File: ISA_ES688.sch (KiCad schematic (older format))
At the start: 104 parts, among them J1 LINE IN, J11 ISA BUS, J2 LINE OUT, J3 Joystick/MIDI, J7 SPKR OUT, J8 MIC, U1 L78L05, U2 74LS14, U7 LM1877, Y1 14.318Mhz

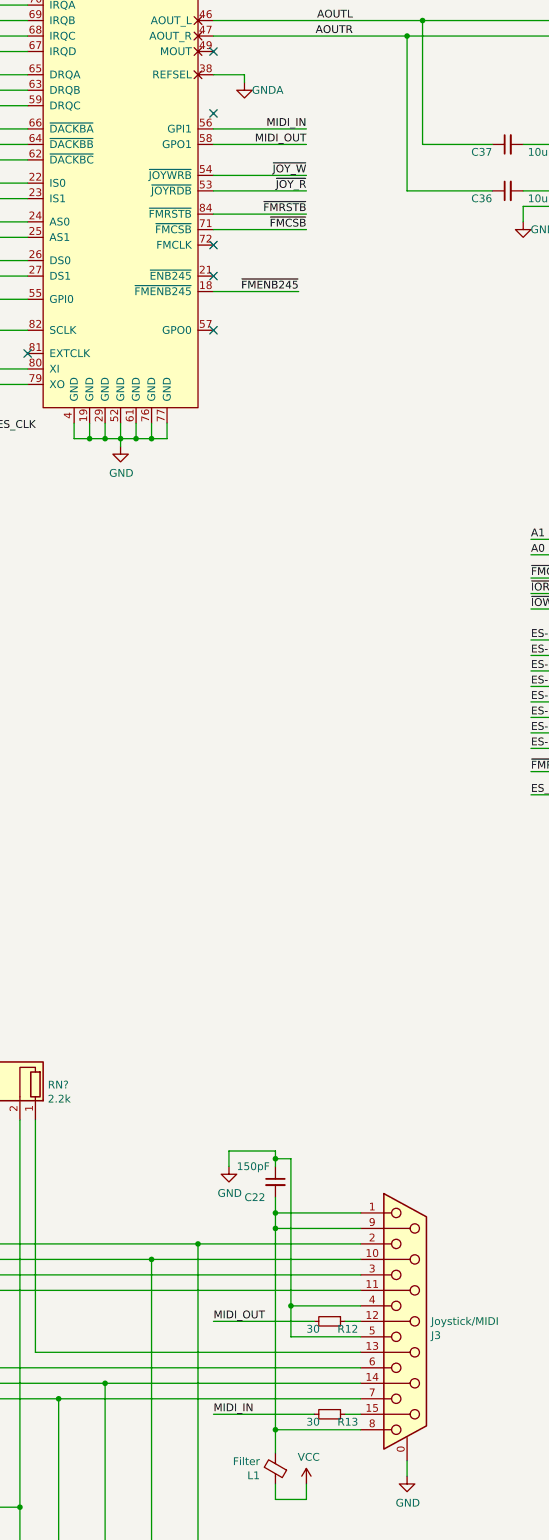
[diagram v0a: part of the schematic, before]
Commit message: Rewire midi connection
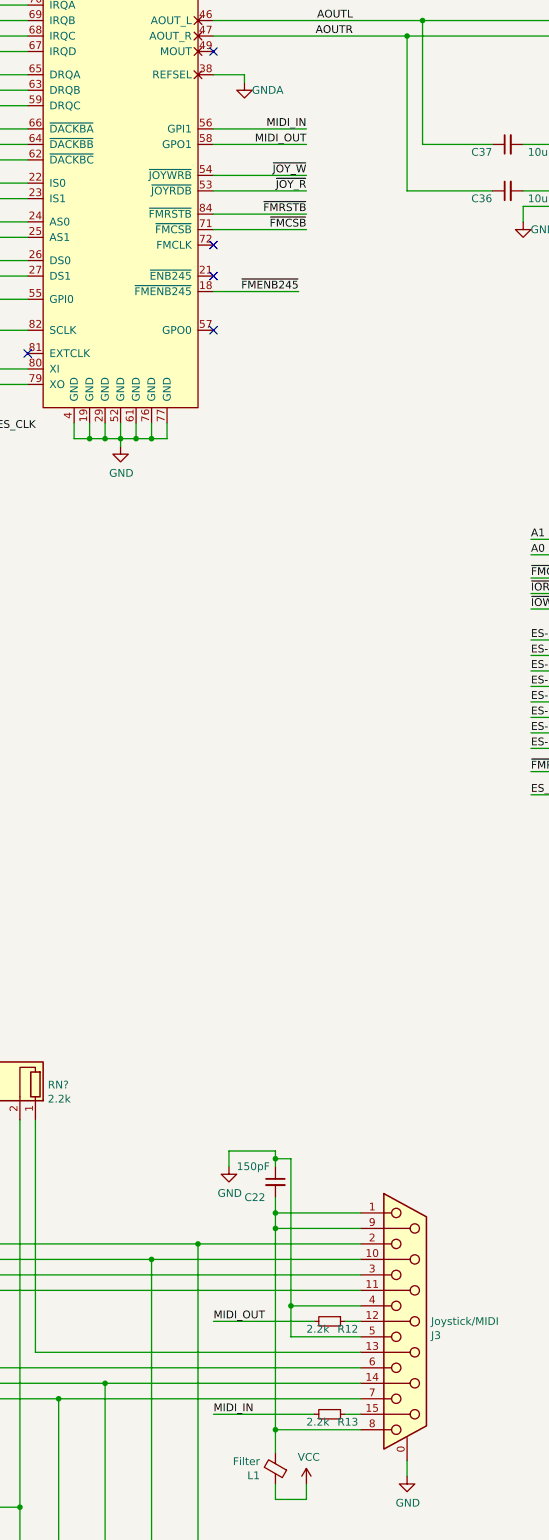
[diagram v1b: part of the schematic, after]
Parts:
- R12, R13: value 30 -> 2.2k
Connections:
- no-connect marks 33 -> 32
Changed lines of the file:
@@
 P 13350 13550
 F 0 "R13" V 13400 13600 50  0000 L CNN
-F 1 "30" V 13400 13400 50  0000 L CNN
+F 1 "2.2k" V 13400 13400 50  0000 L CNN
 F 2 "Resistor_THT:R_Axial_DIN0207_L6.3mm_D2.5mm_P7.62mm_Horizontal" H 13350 13550 50  0001 C CNN
 F 3 "~" H 13350 13550 50  0001 C CNN
@@
 P 13350 12950
 F 0 "R12" V 13400 13000 50  0000 L CNN
-F 1 "30" V 13400 12800 50  0000 L CNN
+F 1 "2.2k" V 13400 12800 50  0000 L CNN
 F 2 "Resistor_THT:R_Axial_DIN0207_L6.3mm_D2.5mm_P7.62mm_Horizontal" H 13350 12950 50  0001 C CNN
 F 3 "~" H 13350 12950 50  0001 C CNN
@@
 Text Notes 20850 10100 0    50   ~ 0
 C24 measured out of circuit as 160nF
-NoConn ~ 12600 5150
 $EndSCHEMATC

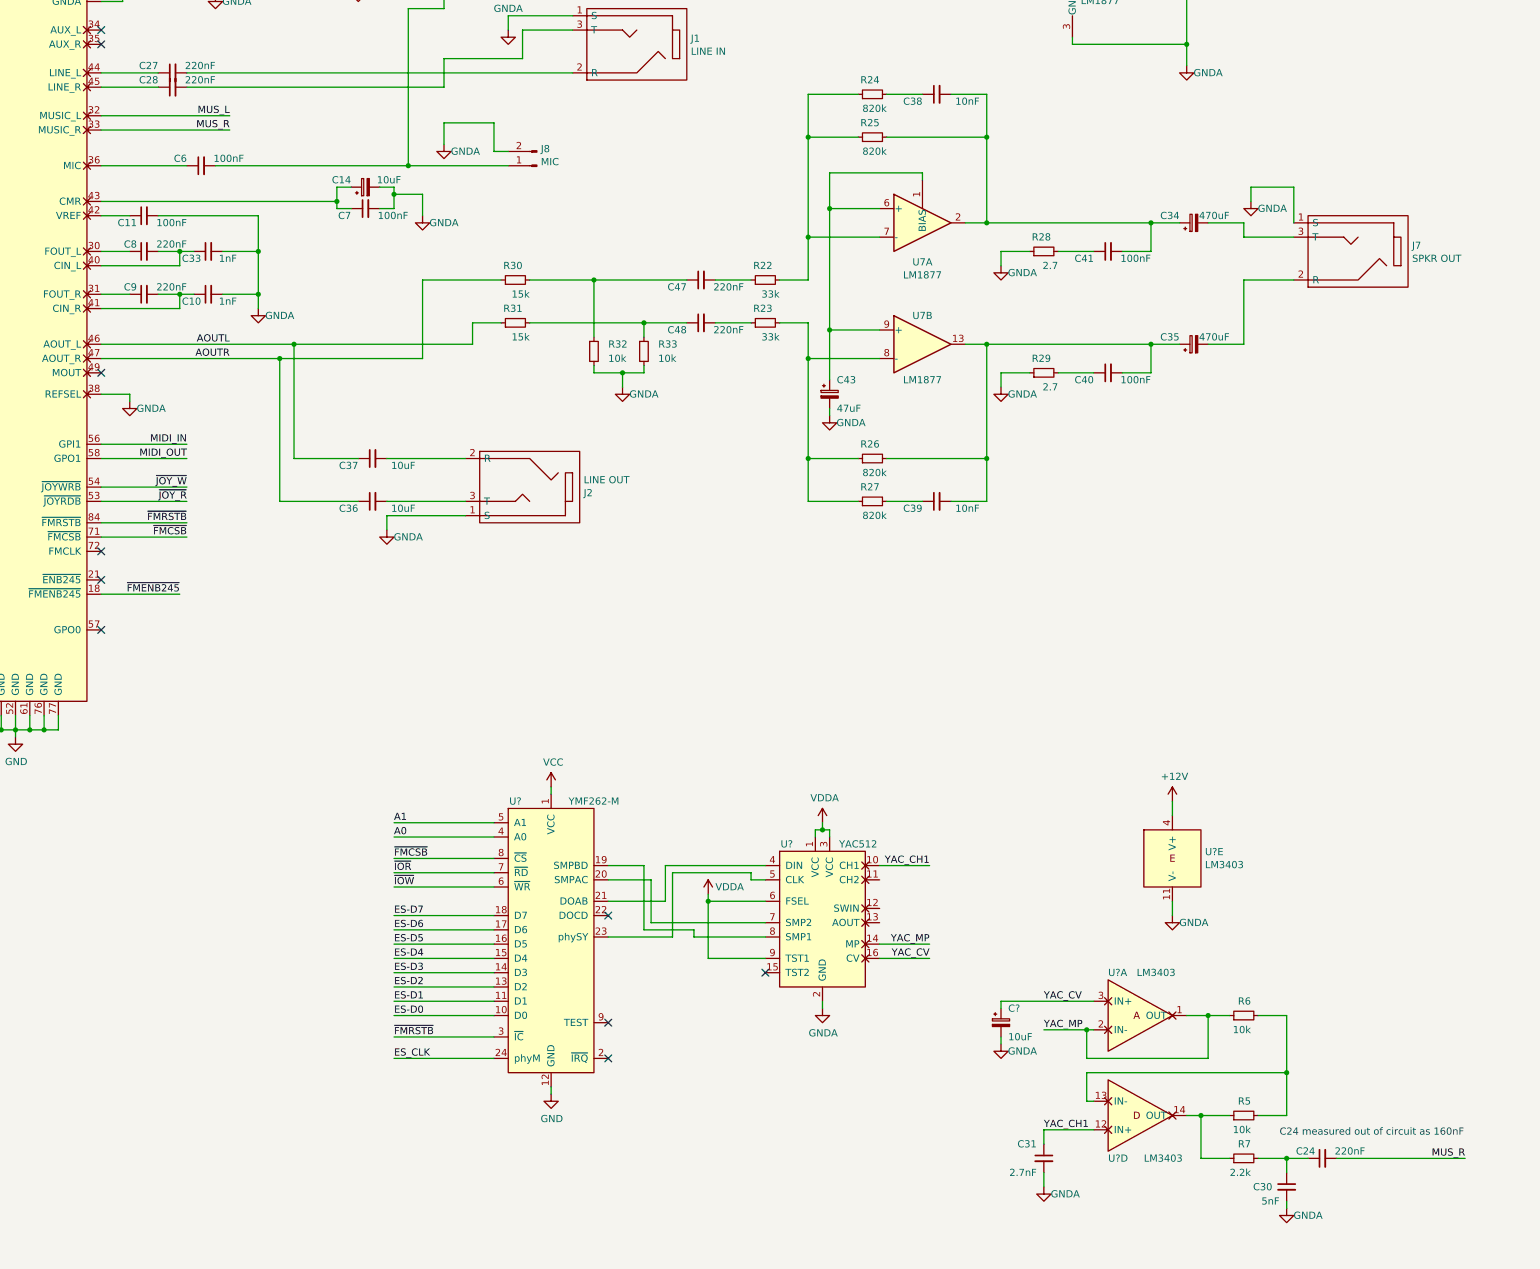
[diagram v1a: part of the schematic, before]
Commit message: Reorganize connections a bit
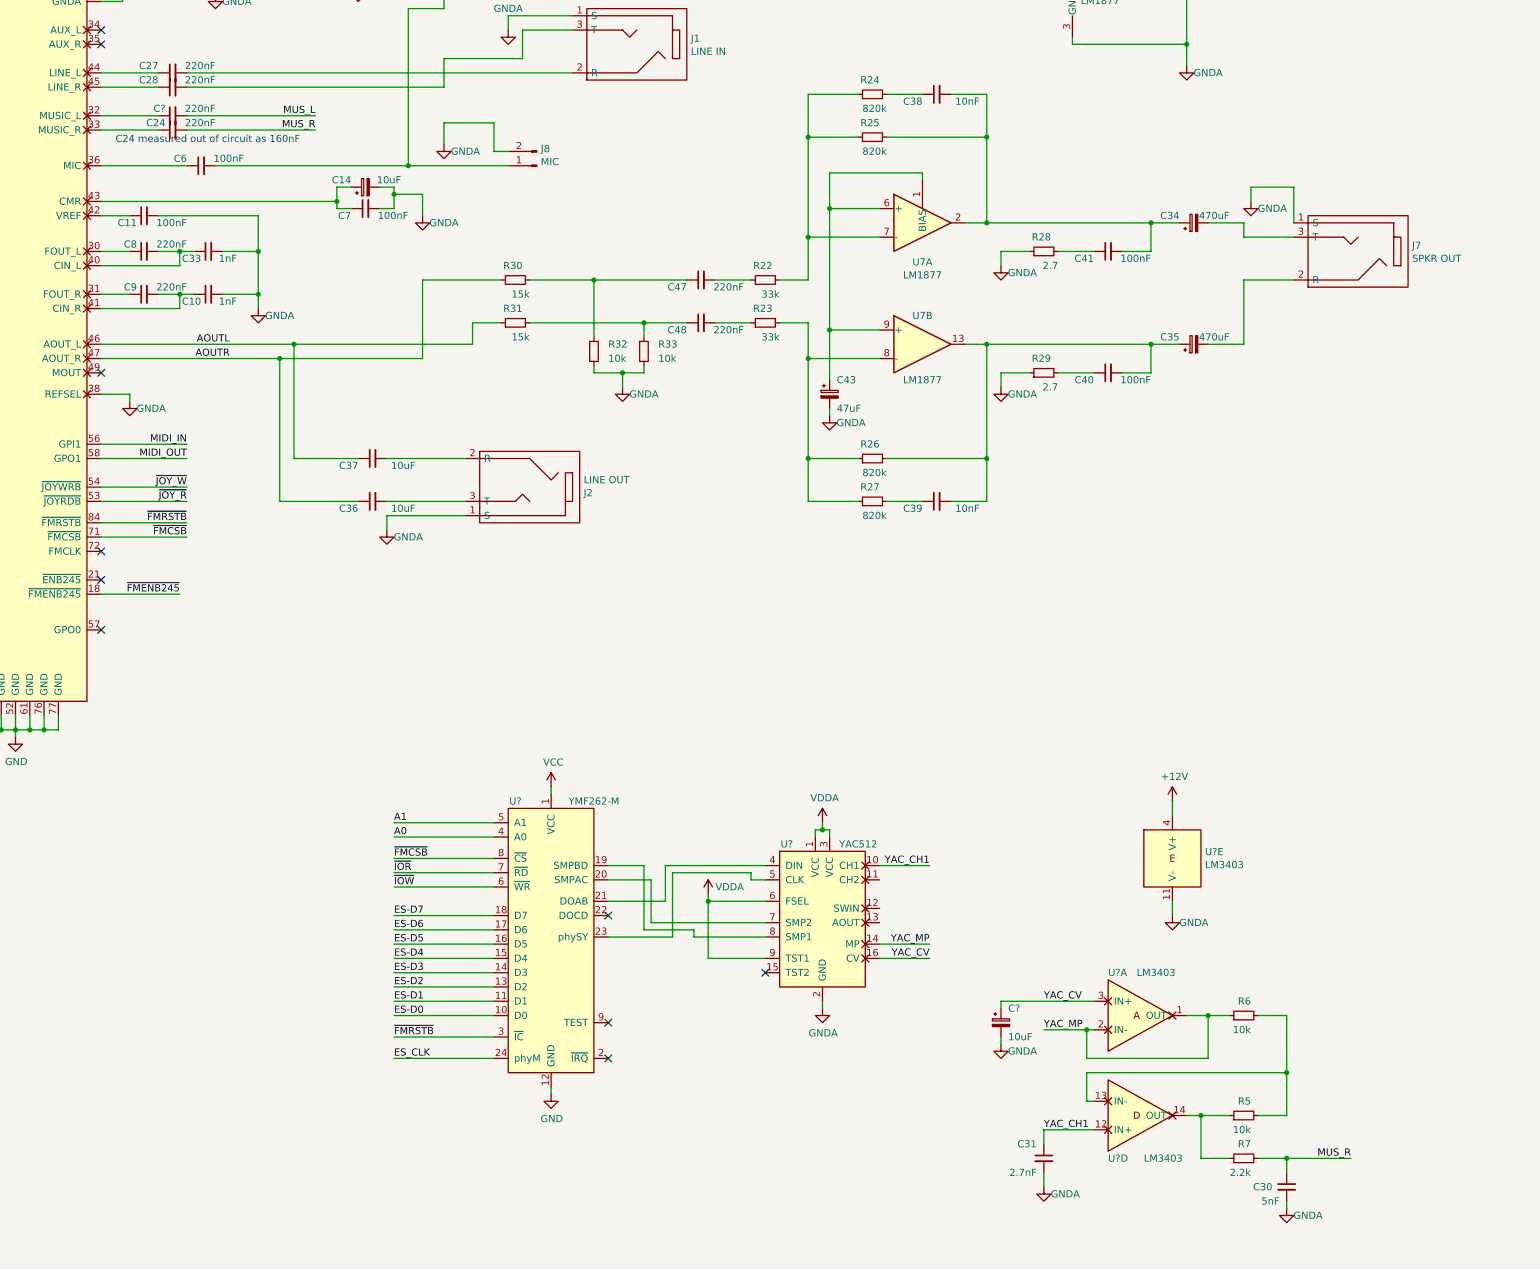
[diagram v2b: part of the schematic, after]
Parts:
- added C?: 220nF, Capacitor_THT:C_Disc_D6.0mm_W2.5mm_P5.00mm, symbol Device:C_Small
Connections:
- net MUS_L: now also C?.2; no longer U?.32 (MUSIC_L)
- net MUS_R: now also C30.1, R7.2; no longer U?.33 (MUSIC_R)
- new net: C?.1, U?.32 (MUSIC_L)
- new net: C24.1, U?.33 (MUSIC_R)
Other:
- moved on the sheet: C24
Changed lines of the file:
@@
 NoConn ~ 12600 2450
 Wire Wire Line
-	12600 2950 13500 2950
-Wire Wire Line
-	12600 3050 13500 3050
-Text Label 13500 2950 2    50   ~ 0
+	13200 2950 14100 2950
+Wire Wire Line
+	13200 3050 14100 3050
+Text Label 14100 2950 2    50   ~ 0
 MUS_L
-Text Label 13500 3050 2    50   ~ 0
+Text Label 14100 3050 2    50   ~ 0
 MUS_R
 NoConn ~ 12600 6200
@@
 L Device:C_Small C24
 U 1 1 62A6A051
-P 21150 10250
-F 0 "C24" V 21100 10300 50  0000 L CNN
-F 1 "220nF" V 21100 9950 50  0000 L CNN
-F 2 "Capacitor_THT:C_Disc_D6.0mm_W2.5mm_P5.00mm" H 21150 10250 50  0001 C CNN
-F 3 "~" H 21150 10250 50  0001 C CNN
-	1    21150 10250
+P 13100 3050
+F 0 "C24" V 13050 3100 50  0000 L CNN
+F 1 "220nF" V 13050 2750 50  0000 L CNN
+F 2 "Capacitor_THT:C_Disc_D6.0mm_W2.5mm_P5.00mm" H 13100 3050 50  0001 C CNN
+F 3 "~" H 13100 3050 50  0001 C CNN
+	1    13100 3050
 	0    -1   1    0
 $EndComp
-Wire Wire Line
-	20900 10250 21050 10250
-Connection ~ 20900 10250
-Wire Wire Line
-	21250 10250 22150 10250
-Text Label 22150 10250 2    50   ~ 0
+Text Label 21350 10250 2    50   ~ 0
 MUS_R
 Wire Wire Line
@@
 Wire Wire Line
 	19200 10050 19200 10150
-Text Notes 20850 10100 0    50   ~ 0
+Text Notes 12700 3150 0    50   ~ 0
 C24 measured out of circuit as 160nF
+$Comp
+L Device:C_Small C?
+U 1 1 61F8B525
+P 13100 2950
+F 0 "C?" V 13050 3000 50  0000 L CNN
+F 1 "220nF" V 13050 2650 50  0000 L CNN
+F 2 "Capacitor_THT:C_Disc_D6.0mm_W2.5mm_P5.00mm" H 13100 2950 50  0001 C CNN
+F 3 "~" H 13100 2950 50  0001 C CNN
+	1    13100 2950
+	0    -1   1    0
+$EndComp
+Wire Wire Line
+	12600 2950 13000 2950
+Wire Wire Line
+	13000 3050 12600 3050
+Wire Wire Line
+	20900 10250 21350 10250
+Connection ~ 20900 10250
 $EndSCHEMATC

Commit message: More OP-AMP circuit
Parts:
- removed JP?: Emulation Mode, symbol Device:Jumper_NO_Small
- removed R?: 10k, Resistor_THT:R_Axial_DIN0207_L6.3mm_D2.5mm_P7.62mm_Horizontal, symbol Device:R_Small
- added C26: 33-68pF, Capacitor_THT:C_Disc_D6.0mm_W2.5mm_P5.00mm, symbol Device:C_Small
- added JP?: Emulation Mode, symbol Jumper:Jumper_3_Open
- added R1: 33, Resistor_THT:R_Axial_DIN0207_L6.3mm_D2.5mm_P7.62mm_Horizontal, symbol Device:R_Small
- C14: value 10uF -> 47uF
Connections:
- net GND: now also JP?.1 (A)
- net GNDA: now also C26.1
- net VCC: now also JP?.3 (B)
- net at U?.55 (GPI0): now also JP?.2 (C)
- net YAC_AOUT: now reaches U?.5 (IN+)
- net YAC_AOUT: now also U?.13 (AOUT), C26.2
- net at U?.6 (IN-): now also U?.7 (OUT), R1.2
- net YAC_CH2: now reaches U?.11 (CH2)
- net YAC_SWIN: now reaches U?.12 (SWIN)
- net YAC_SWIN: now also R1.1
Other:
- note added: "1-2: Sound Blaster v2.11\n2-3: Sound Blaster PRO v3.1"
- note removed: "Defaults to\nSound Blaster PRO"
- moved on the sheet: U?C
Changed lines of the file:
@@
 P 14450 3450
 F 0 "C14" V 14500 3550 50  0000 L CNN
-F 1 "10uF" V 14500 3200 50  0000 L CNN
+F 1 "47uF" V 14500 3200 50  0000 L CNN
 F 2 "Capacitor_THT:CP_Radial_D5.0mm_P2.50mm" H 14450 3450 50  0001 C CNN
 F 3 "~" H 14450 3450 50  0001 C CNN
@@
 	11100 6700 11100 6550
 $Comp
-L Device:R_Small R?
-U 1 1 624E2824
-P 10550 6550
-F 0 "R?" H 10400 6500 50  0000 L CNN
-F 1 "10k" H 10350 6600 50  0000 L CNN
-F 2 "Resistor_THT:R_Axial_DIN0207_L6.3mm_D2.5mm_P7.62mm_Horizontal" H 10550 6550 50  0001 C CNN
-F 3 "~" H 10550 6550 50  0001 C CNN
-	1    10550 6550
-	-1   0    0    1
-$EndComp
-Wire Wire Line
-	11400 6350 10550 6350
-Wire Wire Line
-	10550 6350 10550 6450
-Wire Wire Line
-	10550 6650 10550 6700
-Wire Wire Line
-	10550 6700 10850 6700
-Connection ~ 10850 6700
-$Comp
-L Device:Jumper_NO_Small JP?
-U 1 1 626D2891
-P 10350 6350
-F 0 "JP?" H 10350 6250 50  0000 C CNN
-F 1 "Emulation Mode" H 10350 6444 50  0000 C CNN
-F 2 "" H 10350 6350 50  0001 C CNN
-F 3 "~" H 10350 6350 50  0001 C CNN
-	1    10350 6350
-	1    0    0    -1
-$EndComp
-Wire Wire Line
-	10450 6350 10550 6350
-Connection ~ 10550 6350
-$Comp
 L power:GND #PWR?
 U 1 1 6271B50D
-P 10150 6500
-F 0 "#PWR?" H 10150 6250 50  0001 C CNN
-F 1 "GND" H 10155 6327 50  0000 C CNN
-F 2 "" H 10150 6500 50  0001 C CNN
-F 3 "" H 10150 6500 50  0001 C CNN
-	1    10150 6500
-	1    0    0    -1
-$EndComp
-Wire Wire Line
-	10250 6350 10150 6350
-Wire Wire Line
-	10150 6350 10150 6500
-Text Notes 10050 6500 2    50   ~ 0
-Defaults to\nSound Blaster PRO
+P 9750 7100
+F 0 "#PWR?" H 9750 6850 50  0001 C CNN
+F 1 "GND" H 9755 6927 50  0000 C CNN
+F 2 "" H 9750 7100 50  0001 C CNN
+F 3 "" H 9750 7100 50  0001 C CNN
+	1    9750 7100
+	1    0    0    -1
+$EndComp
 Wire Wire Line
 	11400 4450 10900 4450
@@
 L custom_components:LM3403 U?
 U 3 1 6191F91E
-P 19950 12200
-F 0 "U?" H 19750 12500 50  0000 L CNN
-F 1 "LM3403" H 19950 12500 50  0000 L CNN
-F 2 "" H 19950 12200 50  0001 C CNN
-F 3 "" H 19950 12200 50  0001 C CNN
-	3    19950 12200
+P 19950 12500
+F 0 "U?" H 19750 12800 50  0000 L CNN
+F 1 "LM3403" H 19950 12800 50  0000 L CNN
+F 2 "" H 19950 12500 50  0001 C CNN
+F 3 "" H 19950 12500 50  0001 C CNN
+	3    19950 12500
 	1    0    0    -1
 $EndComp
@@
 	20900 10250 21350 10250
 Connection ~ 20900 10250
+$Comp
+L Jumper:Jumper_3_Open JP?
+U 1 1 62275D16
+P 9750 6750
+F 0 "JP?" V 9796 6837 50  0000 L CNN
+F 1 "Emulation Mode" V 9705 6837 50  0000 L CNN
+F 2 "" H 9750 6750 50  0001 C CNN
+F 3 "~" H 9750 6750 50  0001 C CNN
+	1    9750 6750
+	0    -1   -1   0
+$EndComp
+Wire Wire Line
+	9750 7000 9750 7100
+$Comp
+L power:VCC #PWR?
+U 1 1 625D33F1
+P 9750 6400
+F 0 "#PWR?" H 9750 6250 50  0001 C CNN
+F 1 "VCC" H 9900 6450 50  0000 C CNN
+F 2 "" H 9750 6400 50  0001 C CNN
+F 3 "" H 9750 6400 50  0001 C CNN
+	1    9750 6400
+	1    0    0    -1
+$EndComp
+Wire Wire Line
+	11400 6350 10250 6350
+Wire Wire Line
+	10250 6350 10250 6750
+Wire Wire Line
+	10250 6750 9900 6750
+Wire Wire Line
+	9750 6500 9750 6400
+Text Notes 8550 7050 0    50   ~ 0
+1-2: Sound Blaster v2.11\n2-3: Sound Blaster PRO v3.1
+Wire Wire Line
+	18050 8600 18400 8600
+Text Label 18400 8600 2    50   ~ 0
+YAC_AOUT
+Text Label 18950 11450 0    50   ~ 0
+YAC_AOUT
+Wire Wire Line
+	18950 11450 19500 11450
+$Comp
+L Device:C_Small C26
+U 1 1 62A2E09E
+P 19500 11200
+F 0 "C26" H 19550 11300 50  0000 L CNN
+F 1 "33-68pF" H 19550 11100 50  0000 L CNN
+F 2 "Capacitor_THT:C_Disc_D6.0mm_W2.5mm_P5.00mm" H 19500 11200 50  0001 C CNN
+F 3 "~" H 19500 11200 50  0001 C CNN
+	1    19500 11200
+	-1   0    0    -1
+$EndComp
+Wire Wire Line
+	19500 11300 19500 11450
+Connection ~ 19500 11450
+Wire Wire Line
+	19500 11450 19650 11450
+$Comp
+L power:GNDA #PWR?
+U 1 1 62AAAABD
+P 19150 11000
+F 0 "#PWR?" H 19150 10750 50  0001 C CNN
+F 1 "GNDA" H 19150 10850 50  0000 C CNN
+F 2 "" H 19150 11000 50  0001 C CNN
+F 3 "" H 19150 11000 50  0001 C CNN
+	1    19150 11000
+	1    0    0    -1
+$EndComp
+Wire Wire Line
+	19500 11100 19500 10850
+Wire Wire Line
+	19500 10850 19150 10850
+Wire Wire Line
+	19150 10850 19150 11000
+Wire Wire Line
+	20300 11550 20500 11550
+Wire Wire Line
+	20500 11550 20500 11900
+Wire Wire Line
+	20500 11900 19500 11900
+Wire Wire Line
+	19500 11900 19500 11650
+Wire Wire Line
+	19500 11650 19650 11650
+$Comp
+L Device:R_Small R1
+U 1 1 62CA2E14
+P 19400 11650
+F 0 "R1" V 19500 11600 50  0000 L CNN
+F 1 "33" V 19300 11600 50  0000 L CNN
+F 2 "Resistor_THT:R_Axial_DIN0207_L6.3mm_D2.5mm_P7.62mm_Horizontal" H 19400 11650 50  0001 C CNN
+F 3 "~" H 19400 11650 50  0001 C CNN
+	1    19400 11650
+	0    -1   -1   0
+$EndComp
+Connection ~ 19500 11650
+Wire Wire Line
+	19300 11650 18950 11650
+Text Label 18950 11650 0    50   ~ 0
+YAC_SWIN
+Wire Wire Line
+	18050 8500 18400 8500
+Text Label 18400 8500 2    50   ~ 0
+YAC_SWIN
+Wire Wire Line
+	18050 8300 18400 8300
+Text Label 18400 8300 2    50   ~ 0
+YAC_CH2
 $EndSCHEMATC
